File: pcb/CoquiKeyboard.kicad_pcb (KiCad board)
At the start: 2 copper layers, 307.2 x 79.8 mm, 128 parts, among them P1 USB_C_Plug_USB2.0, SW1 SW_Push, U1 ATmega32U4-AU, Y1 16MHz

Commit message: cleanup
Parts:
- MX26: moved to F.Cu
- moved R1 177.4 mm to (308.7, 6.86)
- moved R2 177.4 mm to (308.7, 9.14)
- moved R4 168.1 mm to (321.4, 11.5)
- moved R3 168.1 mm to (319.0, 11.5)
- moved F1 166.7 mm to (315.3, 10.9)
- moved P1 165.3 mm to (315.5, -5.71)
- moved D23 5.90 mm to (151.3, 28.6)
- turned MX26 to 0 degrees
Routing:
- net GND: track 287.5 -> 258.7 mm
- net Net-(D23-Pad2): track 7.27 -> 0.00 mm
- net D+: track 6.91 -> 0.00 mm
- net D-: track 5.34 -> 0.00 mm
- net Net-(D26-Pad2): track 12.7 -> 7.60 mm
- net VCC: track 4.75 -> 0.00 mm
- net row0: track 300.5 -> 298.7 mm, vias 2 -> 0
- net (no net): track 0.00 -> 0.90 mm, vias 4 -> 0

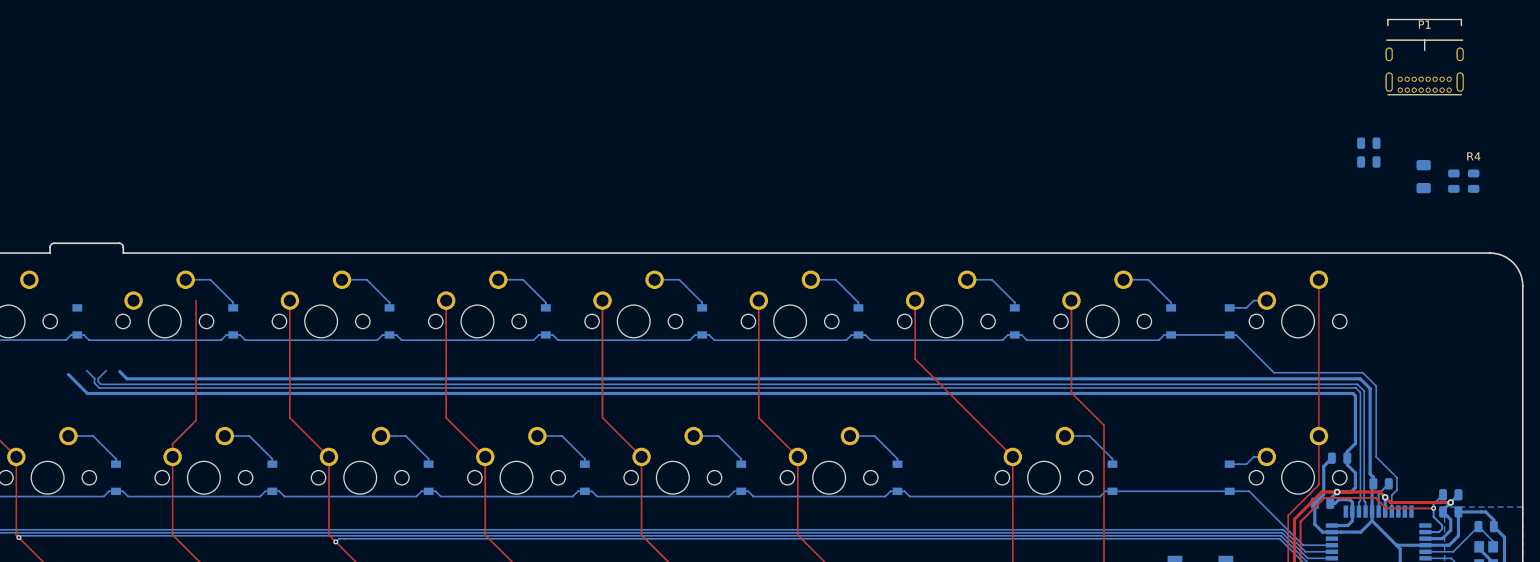
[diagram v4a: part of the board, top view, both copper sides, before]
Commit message: connected remainder of diodes, network closed
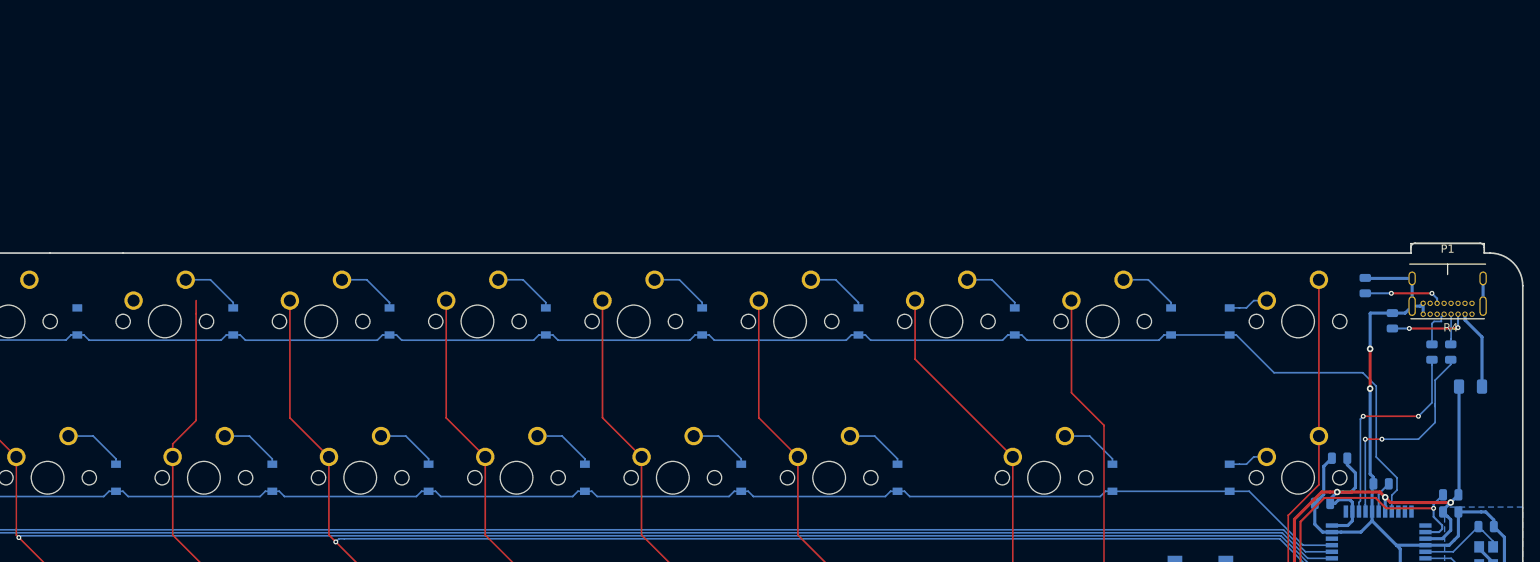
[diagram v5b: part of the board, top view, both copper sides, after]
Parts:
- moved P1 27.4 mm to (318.3, 21.6)
- moved F1 26.2 mm to (321.1, 36.5), turned to 0 degrees
- moved R1 21.8 mm to (311.5, 28.5), turned to 270 degrees
- moved R4 21.0 mm to (318.6, 32.3)
- moved R3 21.0 mm to (316.4, 32.3)
- moved R2 15.1 mm to (308.2, 24.2), turned to 270 degrees
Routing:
- net +5V: track 239.4 -> 86.6 mm
- net /MCU_D-: track 171.3 -> 26.1 mm, vias 0 -> 2
- net /MCU_D+: track 171.3 -> 26.7 mm, vias 0 -> 2
- net GND: track 258.7 -> 135.7 mm, vias 0 -> 2
- net Net-(P1-PadA5): track 0.00 -> 9.75 mm, vias 0 -> 2
- net VCC: track 0.00 -> 9.73 mm
- net Net-(P1-PadB5): track 0.00 -> 9.60 mm, vias 0 -> 2
- net D-: track 0.00 -> 4.88 mm
- net D+: track 0.00 -> 3.70 mm
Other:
- outline, holes or cut-outs redrawn

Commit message: repopulate the BOM file
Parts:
- moved D10 102.2 mm to (124.3, 139.6)
- moved MX13 102.2 mm to (135.1, 139.6)
- moved MX19 102.2 mm to (170.8, 177.7)
- moved R4 102.2 mm to (363.2, 124.3)
- moved C1 102.2 mm to (363.2, 143.7)
- moved C2 102.2 mm to (345.4, 154.3)
- moved C3 102.2 mm to (347.6, 142.7)
- moved C4 102.2 mm to (349.7, 137.2)
- moved C7 102.2 mm to (354.7, 140.3)
- moved D13 102.2 mm to (143.4, 139.6)
- moved D14 102.2 mm to (152.9, 158.6)
- moved D15 102.2 mm to (145.8, 177.7)
- moved D17 102.2 mm to (162.4, 139.6)
- moved D19 102.2 mm to (179.1, 177.7)
- moved D2 102.2 mm to (83.9, 139.6)
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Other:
- rule trace_min: 0.2 -> 0.1

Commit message: complete board for prototyping
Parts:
- moved R1 6.48 mm to (357.3, 126.8), turned to 90 degrees
- moved R3 2.90 mm to (359.5, 126.8)
- moved R4 2.90 mm to (361.8, 126.8)
- moved R2 2.71 mm to (353.3, 118.8), turned to 90 degrees
- moved F1 1.93 mm to (364.4, 127.0), turned to 90 degrees
- moved P1 1.91 mm to (361.3, 114.7)
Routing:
- net GND: track 135.7 -> 144.0 mm
- net Net-(D23-Pad2): track 0.00 -> 7.71 mm
- net VCC: track 9.73 -> 13.3 mm
- net /MCU_D-: track 26.1 -> 22.7 mm
- net /MCU_D+: track 26.7 -> 24.7 mm
- net Net-(P1-PadB5): track 9.60 -> 7.94 mm, vias 2 -> 1
- net D+: track 3.70 -> 5.11 mm
- net colH: track 216.2 -> 217.0 mm
- net D-: track 4.88 -> 5.64 mm
- net Net-(P1-PadA5): track 9.75 -> 9.25 mm, vias 2 -> 1
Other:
- board size 307.2 x 79.8 mm -> 307.2 x 78.6 mm

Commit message: readjust the pcb cutout to compensate for stab footprint
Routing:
- net (no net): track 0.97 -> 0.06 mm
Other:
- board size 307.2 x 78.6 mm -> 307.2 x 79 mm
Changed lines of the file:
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@@
   (general
     (thickness 1.6)
-    (drawings 15)
+    (drawings 14)
     (tracks 886)
     (zones 0)
@@
     (pad "" np_thru_hole circle (at 11.90625 -8.255) (size 3.9878 3.9878) (drill 3.9878) (layers *.Cu *.Mask))
   )
+  (gr_line (start 371.998616 116.188624) (end 371.998616 187.150808) (layer Edge.Cuts) (width 0.2))
+  (gr_line (start 64.817624 183.150312) (end 64.817624 116.188624) (layer Edge.Cuts) (width 0.2))
   (gr_line (start 358.374048 112.188624) (end 201.441728 112.188624) (layer Edge.Cuts) (width 0.2))
   (gr_line (start 367.998616 112.188624) (end 358.374048 112.188624) (layer Edge.Cuts) (width 0.2))
@@
   (gr_line (start 68.817624 112.188624) (end 192.512048 112.188624) (layer Edge.Cuts) (width 0.2))
   (gr_arc (start 367.998616 116.188624) (end 371.998616 116.188624) (angle -90) (layer Edge.Cuts) (width 0.2))
-  (gr_arc (start 367.998616 186.769808) (end 367.998616 190.769808) (angle -90) (layer Edge.Cuts) (width 0.2))
-  (gr_arc (start 321.229912 186.769808) (end 317.229912 186.769808) (angle -90) (layer Edge.Cuts) (width 0.2))
-  (gr_arc (start 68.817624 182.007312) (end 64.817624 182.007312) (angle -90) (layer Edge.Cuts) (width 0.2))
+  (gr_arc (start 367.998616 187.150808) (end 367.998616 191.150808) (angle -90) (layer Edge.Cuts) (width 0.2))
+  (gr_arc (start 321.229912 187.150808) (end 317.229912 187.150808) (angle -90) (layer Edge.Cuts) (width 0.2))
+  (gr_arc (start 68.817624 183.150312) (end 64.817624 183.150312) (angle -90) (layer Edge.Cuts) (width 0.2))
   (gr_arc (start 68.817624 116.188624) (end 68.817624 112.188624) (angle -90) (layer Edge.Cuts) (width 0.2))
-  (gr_line (start 64.817624 182.007312) (end 64.817624 116.188624) (layer Edge.Cuts) (width 0.2))
-  (gr_line (start 317.229912 186.007312) (end 68.817624 186.007312) (layer Edge.Cuts) (width 0.2))
-  (gr_line (start 317.229912 186.769808) (end 317.229912 186.007312) (layer Edge.Cuts) (width 0.2))
-  (gr_line (start 367.998616 190.769808) (end 321.229912 190.769808) (layer Edge.Cuts) (width 0.2))
-  (gr_line (start 371.998616 116.188624) (end 371.998616 186.769808) (layer Edge.Cuts) (width 0.2))
-  (segment (start 44.236375 91.693) (end 44.875276 92.331901) (width 0.2032) (layer B.Cu) (net 0))
+  (gr_line (start 317.229912 187.150312) (end 68.817624 187.150312) (layer Edge.Cuts) (width 0.2))
+  (gr_line (start 367.998616 191.150808) (end 321.229912 191.150808) (layer Edge.Cuts) (width 0.2))
   (segment (start 362.458 119.682) (end 362.414 119.638) (width 0.2032) (layer B.Cu) (net 0))
   (segment (start 349.867912 146.195624) (end 348.736912 146.195624) (width 0.381) (layer B.Cu) (net 1))
@@
   (segment (start 353.314 119.761) (end 356.95 119.761) (width 0.381) (layer B.Cu) (net 1))
   (segment (start 357.335 119.456) (end 356.99 119.801) (width 0.381) (layer F.Cu) (net 1))
-  (segment (start 358.335 119.456) (end 357.335 119.456) (width 0.381) (layer F.Cu) (net 1))
   (segment (start 353.395116 128.708532) (end 353.395116 126.410884) (width 0.381) (layer F.Cu) (net 1))
   (segment (start 353.395116 126.410884) (end 353.395116 126.410884) (width 0.381) (layer F.Cu) (net 1))
@@
   (segment (start 357.251 127.762) (end 356.451 127.762) (width 0.381) (layer B.Cu) (net 1))
   (segment (start 353.395116 125.521884) (end 353.395116 119.842116) (width 0.381) (layer B.Cu) (net 1))
+  (segment (start 357.99 119.801) (end 358.335 119.456) (width 0.381) (layer B.Cu) (net 1))
+  (segment (start 356.99 119.801) (end 357.99 119.801) (width 0.381) (layer B.Cu) (net 1))
   (segment (start 360.136912 146.995624) (end 362.19472 146.995624) (width 0.25) (layer B.Cu) (net 2))
   (segment (start 362.19472 146.995624) (end 363.217764 145.97258) (width 0.25) (layer B.Cu) (net 2))
